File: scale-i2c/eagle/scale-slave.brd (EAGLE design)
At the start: 49.5 x 49.5 mm, 39 parts, among them CON1 SPI, IC1 MCP1703CB, J2 RJ12RIGHTANGLE-I2C, J3 RJ12RIGHTANGLE-I2C, U1 ATMEGA328P_TQFP, U2 HX711, X1 8MHz

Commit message: final scale
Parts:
- removed SJ1: A0, jumper:SJ
- added C13: 100nF, rcl:C0805K
- added R18, R19: 1M, rcl:R0805
- moved WGT 34.3 mm to (41.9, 47.0), turned to 180 degrees
- moved CU2 12.1 mm to (38.1, 33.0), turned to 90 degrees
- moved SJ4 10.0 mm to (45.7, 33.0), turned to 90 degrees
- moved SJ3 7.01 mm to (26.0, 45.1), turned to 180 degrees
- moved BJ1 5.72 mm to (21.0, 42.5), turned to 0 degrees
- moved RK5 5.43 mm to (26.0, 42.5)
- moved RL1 5.24 mm to (41.9, 41.9), turned to 90 degrees
- moved CU1 4.96 mm to (26.0, 37.5), turned to 180 degrees
- moved 8.2K 4.45 mm to (35.6, 33.0)
- moved C10 4.07 mm to (43.2, 33.0), turned to 90 degrees
- moved C12 4.02 mm to (43.2, 38.1)
- moved C11 3.81 mm to (40.6, 33.0)
- moved C9 2.62 mm to (26.0, 40.0), turned to 180 degrees
- moved RL2 2.62 mm to (45.1, 41.9), turned to 90 degrees
- moved 20K 0.90 mm to (33.0, 33.0), turned to 270 degrees
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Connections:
- net +5V: now also R18.2
- net A6: now also C13.2, R18.1, R19.2; no longer SJ1.1
- net GND: now also C13.1, R19.1; no longer SJ1.2
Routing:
- net A-: track 35.7 -> 7.16 mm
- net A1: track 0.00 -> 26.2 mm, vias 0 -> 2
- net A0: track 0.00 -> 25.4 mm, vias 0 -> 2
- net A6: track 5.03 -> 27.9 mm, vias 1 -> 2
- net A3: track 16.4 -> 0.88 mm, vias 2 -> 0
- net LGND: track 30.6 -> 18.7 mm
- net N$41: track 20.2 -> 8.47 mm, vias 2 -> 0
- net +5V: track 56.9 -> 66.6 mm, vias 0 -> 1
- net A+: track 0.00 -> 7.43 mm
- net 3.3V: track 11.5 -> 18.5 mm
- net N$20: track 14.9 -> 9.89 mm
- net GND: track 38.9 -> 43.3 mm, vias 13 -> 17
- net N$39: track 10.2 -> 6.04 mm
- net N$38: track 13.1 -> 17.1 mm, vias 2 -> 0
- net CN3: track 11.5 -> 8.80 mm, vias 0 -> 1
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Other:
- board text added: "Slave I2C - Weight V1.0.0"
- board text removed: "Slave I2C - Meteo V1.0.0"

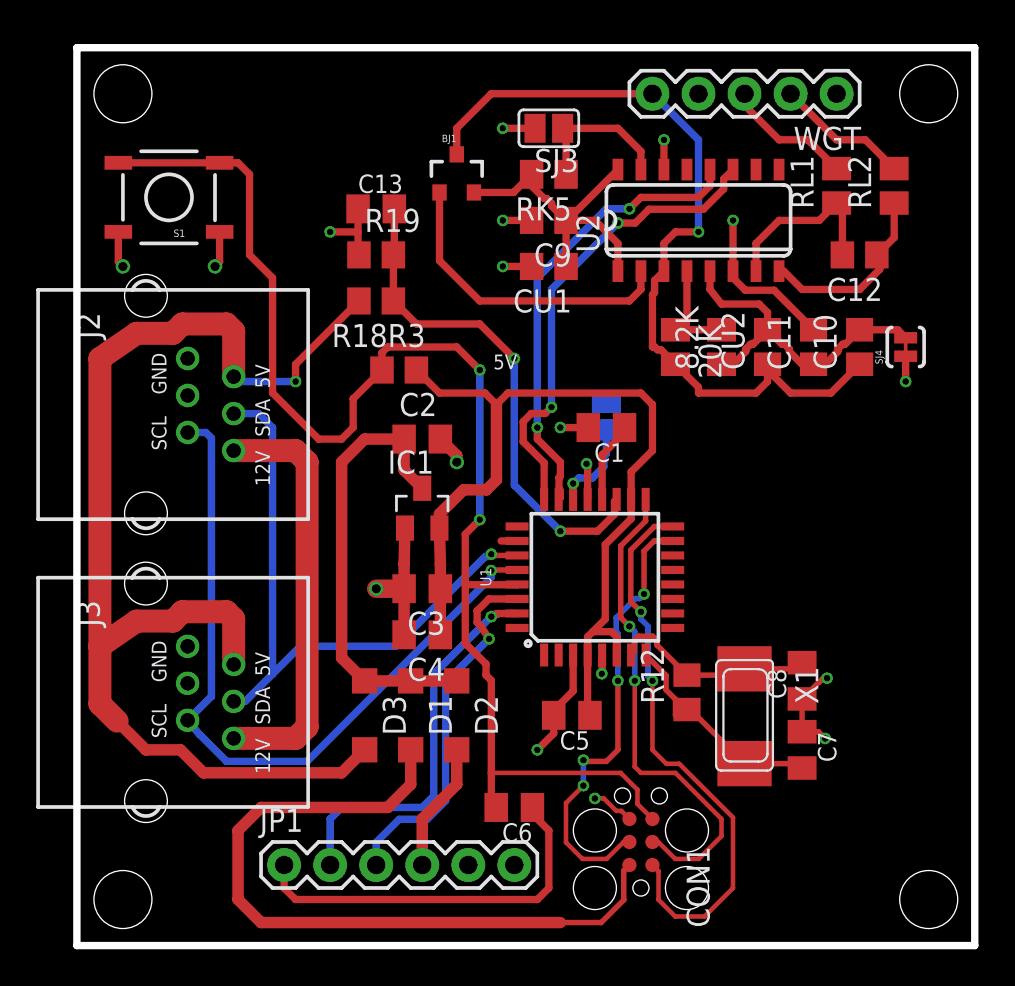
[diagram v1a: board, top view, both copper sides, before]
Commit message: fix the +3.3V
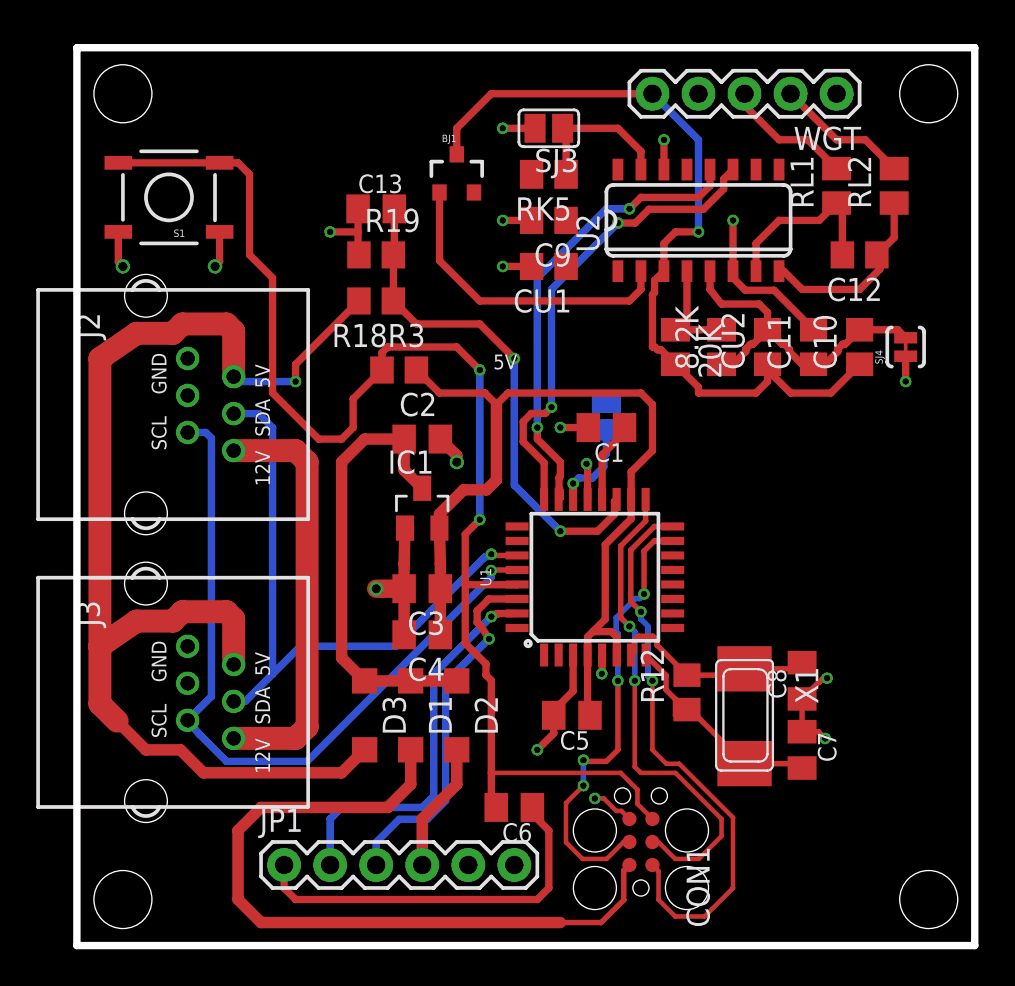
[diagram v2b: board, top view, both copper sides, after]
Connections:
- removed net VCC: C3.1, C4.1, C5.1, IC1.2, R3.2, U1.18, U1.4, U1.6
- net 3.3V: now also C3.1, C4.1, C5.1, IC1.2, R3.2, U1.18, U1.4, U1.6
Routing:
- net VCC: track 50.2 -> 0.00 mm
- net 3.3V: track 18.5 -> 50.2 mm
- net A3: track 0.88 -> 0.00 mm
- added copper zone on layer 1, net 3.3V
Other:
- board text added: "Slave I2C - Weight V1.0.1"
- board text removed: "Slave I2C - Weight V1.0.0"
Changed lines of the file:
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@@
 <?xml version="1.0" encoding="utf-8"?>
 <!DOCTYPE eagle SYSTEM "eagle.dtd">
-<eagle version="9.0.1">
+<eagle version="9.1.0">
 <drawing>
 <settings>
@@
 <layer number="43" name="vRestrict" color="2" fill="10" visible="no" active="yes"/>
 <layer number="44" name="Drills" color="7" fill="1" visible="no" active="yes"/>
-<layer number="45" name="Holes" color="7" fill="1" visible="no" active="yes"/>
+<layer number="45" name="Holes" color="7" fill="1" visible="yes" active="yes"/>
 <layer number="46" name="Milling" color="3" fill="1" visible="no" active="yes"/>
 <layer number="47" name="Measures" color="7" fill="1" visible="no" active="yes"/>
@@
 <hole x="46.99" y="46.99" drill="3.2"/>
 <hole x="46.99" y="2.54" drill="3.2"/>
-<text x="48.895" y="39.37" size="1.778" layer="28" rot="MR270">Slave I2C - Weight V1.0.0</text>
-<text x="48.895" y="11.43" size="1.778" layer="27" rot="R90">Slave I2C - Weight V1.0.0</text>
+<text x="48.895" y="39.37" size="1.778" layer="28" rot="MR270">Slave I2C - Weight V1.0.1</text>
+<text x="48.895" y="11.43" size="1.778" layer="27" rot="R90">Slave I2C - Weight V1.0.1</text>
 <rectangle x1="65.9384" y1="15.9004" x2="66.04" y2="15.9512" layer="200"/>
 <rectangle x1="67.2592" y1="15.9004" x2="67.3608" y2="15.9512" layer="200"/>
@@
 <param name="checkStop" value="0"/>
 <param name="checkValues" value="0"/>
+<param name="checkNames" value="1"/>
+<param name="checkWireStubs" value="1"/>
+<param name="checkPolygonWidth" value="0"/>
 <param name="useDiameter" value="13"/>
 <param name="maxErrors" value="50"/>
@@
 <wire x1="6.745" y1="11.67" x2="8.255" y2="10.16" width="0.4064" layer="16"/>
 <wire x1="6.11" y1="12.43" x2="6.745" y2="11.67" width="0.4064" layer="16"/>
-<wire x1="22.86" y1="20.6852" x2="22.8948" y2="20.72" width="0.4064" layer="1"/>
 <via x="22.86" y="20.6852" extent="1-16" drill="0.35"/>
 <wire x1="22.86" y1="20.32" x2="22.86" y2="20.6852" width="0.4064" layer="16"/>
@@
 <wire x1="20.955" y1="33.02" x2="22.225" y2="31.75" width="0.4064" layer="1"/>
 </signal>
-<signal name="VCC">
-<contactref element="C3" pad="1"/>
-<contactref element="C4" pad="1"/>
-<contactref element="IC1" pad="2"/>
-<contactref element="R3" pad="2"/>
-<contactref element="C5" pad="1"/>
-<wire x1="20" y1="23.03" x2="20.05" y2="21.075" width="0.635" layer="1"/>
-<wire x1="20.05" y1="19.685" x2="20.05" y2="21.075" width="0.635" layer="1"/>
-<wire x1="20.05" y1="17.145" x2="20.05" y2="19.685" width="0.635" layer="1"/>
-<wire x1="23.14575" y1="25.69016875" x2="22.59568125" y2="25.1401" width="0.635" layer="1"/>
-<wire x1="23.14575" y1="29.845" x2="23.14575" y2="25.69016875" width="0.635" layer="1"/>
-<wire x1="28.175" y1="12.83" x2="28.305" y2="12.7" width="0.4064" layer="1"/>
-<wire x1="30.575" y1="26.13" x2="31.75" y2="27.305" width="0.4064" layer="1"/>
-<wire x1="31.75" y1="27.305" x2="31.75" y2="29.845" width="0.4064" layer="1"/>
-<wire x1="31.75" y1="29.845" x2="31.115" y2="30.48" width="0.4064" layer="1"/>
-<wire x1="23.78075" y1="30.48" x2="23.14575" y2="29.845" width="0.4064" layer="1"/>
-<wire x1="31.115" y1="30.48" x2="23.78075" y2="30.48" width="0.4064" layer="1"/>
-<contactref element="U1" pad="6"/>
-<contactref element="U1" pad="4"/>
-<contactref element="U1" pad="18"/>
-<wire x1="28.175" y1="12.83" x2="28.175" y2="16.0274" width="0.4064" layer="1"/>
-<wire x1="29.775" y1="16.0274" x2="29.775" y2="17.03085" width="0.4064" layer="1"/>
-<wire x1="29.775" y1="17.03085" x2="29.4894" y2="17.31645" width="0.4064" layer="1"/>
-<wire x1="28.4607" y1="17.31645" x2="29.4894" y2="17.31645" width="0.4064" layer="1"/>
-<wire x1="28.175" y1="16.0274" x2="28.175" y2="17.03075" width="0.4064" layer="1"/>
-<wire x1="28.175" y1="17.03075" x2="28.4607" y2="17.31645" width="0.4064" layer="1"/>
-<wire x1="30.575" y1="26.13" x2="30.575" y2="24.6126" width="0.4064" layer="1"/>
-<wire x1="30.575" y1="24.6126" x2="30.575" y2="23.54555" width="0.4064" layer="1"/>
-<wire x1="30.575" y1="23.54555" x2="29.1465" y2="22.11705" width="0.4064" layer="1"/>
-<wire x1="29.1465" y1="22.11705" x2="29.1465" y2="18.00225" width="0.4064" layer="1"/>
-<wire x1="29.1465" y1="18.00225" x2="28.4607" y2="17.31645" width="0.4064" layer="1"/>
-<wire x1="23.14575" y1="29.845" x2="22.51075" y2="30.48" width="0.4064" layer="1"/>
-<wire x1="20" y1="23.81" x2="20" y2="23.03" width="0.635" layer="1"/>
-<wire x1="22.59568125" y1="25.1401" x2="21.3301" y2="25.1401" width="0.635" layer="1"/>
-<wire x1="21.3301" y1="25.1401" x2="20" y2="23.81" width="0.635" layer="1"/>
-<wire x1="20" y1="30.48" x2="18.73" y2="31.75" width="0.4064" layer="1"/>
-<wire x1="22.51075" y1="30.48" x2="20" y2="30.48" width="0.4064" layer="1"/>
-</signal>
 <signal name="N$16">
 </signal>
@@
 <signal name="A3">
 <contactref element="U1" pad="26"/>
-<wire x1="24.2824" y1="22.32" x2="23.4" y2="22.32" width="0.4064" layer="1"/>
 </signal>
 <signal name="A2">
@@
 </signal>
 <signal name="3.3V" class="1">
-<contactref element="BJ1" pad="2"/>
-<contactref element="U2" pad="1"/>
-<contactref element="U2" pad="16"/>
 <contactref element="RK5" pad="2"/>
+<contactref element="BJ1" pad="2"/>
+<contactref element="C3" pad="1"/>
+<contactref element="C4" pad="1"/>
+<contactref element="IC1" pad="2"/>
+<contactref element="R3" pad="2"/>
+<contactref element="C5" pad="1"/>
+<wire x1="20" y1="23.03" x2="20.05" y2="21.075" width="0.635" layer="1"/>
+<wire x1="20.05" y1="19.685" x2="20.05" y2="21.075" width="0.635" layer="1"/>
+<wire x1="20.05" y1="17.145" x2="20.05" y2="19.685" width="0.635" layer="1"/>
+<wire x1="23.14575" y1="25.69016875" x2="22.59568125" y2="25.1401" width="0.635" layer="1"/>
+<wire x1="23.14575" y1="29.845" x2="23.14575" y2="25.69016875" width="0.635" layer="1"/>
+<wire x1="28.175" y1="12.83" x2="28.305" y2="12.7" width="0.4064" layer="1"/>
+<wire x1="30.575" y1="26.13" x2="31.75" y2="27.305" width="0.4064" layer="1"/>
+<wire x1="31.75" y1="27.305" x2="31.75" y2="29.845" width="0.4064" layer="1"/>
+<wire x1="31.75" y1="29.845" x2="31.115" y2="30.48" width="0.4064" layer="1"/>
+<wire x1="23.78075" y1="30.48" x2="23.14575" y2="29.845" width="0.4064" layer="1"/>
+<wire x1="31.115" y1="30.48" x2="23.78075" y2="30.48" width="0.4064" layer="1"/>
+<contactref element="U1" pad="6"/>
+<contactref element="U1" pad="4"/>
+<contactref element="U1" pad="18"/>
+<wire x1="28.175" y1="12.83" x2="28.175" y2="16.0274" width="0.4064" layer="1"/>
+<wire x1="29.775" y1="16.0274" x2="29.775" y2="17.03085" width="0.4064" layer="1"/>
+<wire x1="29.775" y1="17.03085" x2="29.4894" y2="17.31645" width="0.4064" layer="1"/>
+<wire x1="28.4607" y1="17.31645" x2="29.4894" y2="17.31645" width="0.4064" layer="1"/>
+<wire x1="28.175" y1="16.0274" x2="28.175" y2="17.03075" width="0.4064" layer="1"/>
+<wire x1="28.175" y1="17.03075" x2="28.4607" y2="17.31645" width="0.4064" layer="1"/>
+<wire x1="30.575" y1="26.13" x2="30.575" y2="24.6126" width="0.4064" layer="1"/>
+<wire x1="30.575" y1="24.6126" x2="30.575" y2="23.54555" width="0.4064" layer="1"/>
+<wire x1="30.575" y1="23.54555" x2="29.1465" y2="22.11705" width="0.4064" layer="1"/>
+<wire x1="29.1465" y1="22.11705" x2="29.1465" y2="18.00225" width="0.4064" layer="1"/>
+<wire x1="29.1465" y1="18.00225" x2="28.4607" y2="17.31645" width="0.4064" layer="1"/>
+<wire x1="23.14575" y1="29.845" x2="22.51075" y2="30.48" width="0.4064" layer="1"/>
+<wire x1="20" y1="23.81" x2="20" y2="23.03" width="0.635" layer="1"/>
+<wire x1="22.59568125" y1="25.1401" x2="21.3301" y2="25.1401" width="0.635" layer="1"/>
+<wire x1="21.3301" y1="25.1401" x2="20" y2="23.81" width="0.635" layer="1"/>
+<wire x1="20" y1="30.48" x2="18.73" y2="31.75" width="0.4064" layer="1"/>
+<wire x1="22.51075" y1="30.48" x2="20" y2="30.48" width="0.4064" layer="1"/>
 <contactref element="C9" pad="1"/>
 <contactref element="CU1" pad="1"/>
-<wire x1="26.985" y1="37.465" x2="26.985" y2="40.005" width="0.4064" layer="1"/>
-<wire x1="25.085" y1="42.545" x2="25.085" y2="41.905" width="0.4064" layer="1"/>
-<wire x1="25.085" y1="41.905" x2="25.7818" y2="41.2082" width="0.4064" layer="1"/>
-<wire x1="25.7818" y1="41.2082" x2="25.92271875" y2="41.2082" width="0.4064" layer="1"/>
-<wire x1="25.92271875" y1="41.2082" x2="26.1882" y2="40.94271875" width="0.4064" layer="1"/>
-<wire x1="26.1882" y1="40.94271875" x2="26.1882" y2="40.8018" width="0.4064" layer="1"/>
-<wire x1="26.1882" y1="40.8018" x2="26.985" y2="40.005" width="0.4064" layer="1"/>
-<wire x1="26.985" y1="40.005" x2="27.045" y2="40.005" width="0.4064" layer="1"/>
-<wire x1="27.045" y1="40.005" x2="29.845" y2="42.805" width="0.4064" layer="1"/>
-<wire x1="26.985" y1="40.005" x2="28.575" y2="40.005" width="0.4064" layer="1"/>
-<wire x1="28.575" y1="40.005" x2="29.845" y2="38.735" width="0.4064" layer="1"/>
-<wire x1="29.845" y1="38.735" x2="29.845" y2="37.205" width="0.4064" layer="1"/>
-<wire x1="21.905" y1="41.545" x2="24.085" y2="41.545" width="0.4064" layer="1"/>
-<wire x1="24.085" y1="41.545" x2="25.085" y2="42.545" width="0.4064" layer="1"/>
+<contactref element="U2" pad="1"/>
+<contactref element="U2" pad="16"/>
+<polygon width="0.1524" layer="1">
+<vertex x="0" y="49.53"/>
+<vertex x="49.53" y="49.53"/>
+<vertex x="49.53" y="0"/>
+<vertex x="0" y="0"/>
+</polygon>
 </signal>
 <signal name="N$38">
@@
 </signal>
 </signals>
+<mfgpreviewcolors>
+<mfgpreviewcolor name="soldermaskcolor" color="0xC8008000"/>
+<mfgpreviewcolor name="silkscreencolor" color="0xFFFEFEFE"/>
+<mfgpreviewcolor name="backgroundcolor" color="0xFF282828"/>
+<mfgpreviewcolor name="coppercolor" color="0xFFFFBF00"/>
+<mfgpreviewcolor name="substratecolor" color="0xFF786E46"/>
+</mfgpreviewcolors>
 </board>
 </drawing>
